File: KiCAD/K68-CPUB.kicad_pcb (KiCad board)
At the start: 2 copper layers, 100 x 100 mm, 64 parts, among them J1 PIA Con, J2 SBC68 BUS, J3 SERIAL COn, J4 Barrel_Jack_Switch, SW1 SW_SPDT, SW2 BOARD SW, SW3 ECHO SW, U1 74LS123, U10 74LS244, U11 74LS244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

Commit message: ガーバーデータ(仮) 生成
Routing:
- net GND: track 28.2 -> 613.9 mm, vias 0 -> 1
- net VCC: track 38.0 -> 432.9 mm, vias 0 -> 1
- net /D1: track 0.00 -> 259.9 mm, vias 0 -> 2
- net /D2: track 0.00 -> 223.2 mm, vias 0 -> 3
- net /D5: track 0.00 -> 212.1 mm, vias 0 -> 3
- net /~RES: track 0.00 -> 198.2 mm, vias 0 -> 3
- net /A0: track 0.00 -> 197.9 mm, vias 0 -> 2
- net /A1: track 0.00 -> 192.0 mm, vias 0 -> 1
- net /A4: track 0.00 -> 187.5 mm, vias 0 -> 4
- net /A2: track 0.00 -> 180.1 mm, vias 0 -> 2
- net /A15: track 0.00 -> 171.6 mm, vias 0 -> 2
- net /D0: track 0.00 -> 171.1 mm, vias 0 -> 4
- net /A7: track 0.00 -> 170.5 mm, vias 0 -> 4
- net /A13: track 0.00 -> 169.8 mm, vias 0 -> 4
- net /R~W: track 0.00 -> 167.3 mm, vias 0 -> 5
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- added copper zone on B.Cu, net GND
- added copper zone on F.Cu, net GND
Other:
- board text added: "28C256 (256k bit EEPROM)"
- board text added: "628128 (1M bit SRAM)"
- board text added: "74LS123"
- board text added: "74LS244"
- board text added: "74LS245"
- board text added: "MC14536"

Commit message: 基板裏面シルク追加・ガーバーデータ再作成
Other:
- board text added: "MC6800 CPU Board [K68-CPUB] REV1 KUNI-NET 2021"
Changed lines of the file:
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@@
   (general
     (thickness 1.6)
-    (drawings 18)
+    (drawings 19)
     (tracks 3065)
     (zones 0)
@@
     )
   )
+  (gr_text "MC6800 CPU Board \n[K68-CPUB] REV1\n\nKUNI-NET 2021" (at 198.5 140) (layer B.SilkS)
+    (effects (font (size 2 2) (thickness 0.2)) (justify left mirror))
+  )
   (gr_text 74LS00 (at 113.9 130.8 270) (layer F.SilkS)

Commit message: 基板パターン修正中...
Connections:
- net /DBE renamed /PH2
- net /R~W renamed /R~{W}
- net /~HALT renamed /~{HALT}
- net /~IRQ renamed /~{IRQ}
- net /~NMI renamed /~{NMI}
- net /~RAMCE renamed /~{RAMCE}
- net /~RD renamed /~{RD}
- net /~RES renamed /~{RES}
- net /~WR renamed /~{WR}
- C4 pad 1: Net-(C4-Pad1) -> Net-(U1B-RCext)
- C4 pad 2: Net-(C4-Pad2) -> Net-(U1B-Cext)
- J1 pad 1: (no net) -> unconnected-(J1-Pin_1-Pad1)
- J1 pad 2: (no net) -> unconnected-(J1-Pin_2-Pad2)
- J2 pad 10: /D7n -> /D7
- J2 pad 11: /A0n -> /A0
- J2 pad 12: /A1n -> /A1
- J2 pad 13: /A2n -> /A2
- J2 pad 14: /A3n -> /A3
- J2 pad 15: /A4n -> /A4
- J2 pad 16: /A5n -> /A5
- J2 pad 17: /A6n -> /A6
- J2 pad 18: /A7n -> /A7
- J2 pad 19: /A8n -> /A8
- J2 pad 20: /A9n -> /A9
- J2 pad 21: /A10n -> /A10
- J2 pad 22: /A11n -> /A11
- J2 pad 23: /A12n -> /A12
- J2 pad 24: /A13n -> /A13
- J2 pad 25: /A14n -> /A14
- J2 pad 26: /A15n -> /A15
- J2 pad 3: /D0n -> /D0
- J2 pad 32: (no net) -> unconnected-(J2-Pin_32-Pad32)
- J2 pad 34: (no net) -> unconnected-(J2-Pin_34-Pad34)
- J2 pad 36: (no net) -> unconnected-(J2-Pin_36-Pad36)
- J2 pad 4: /D1n -> /D1
- J2 pad 5: /D2n -> /D2
- J2 pad 6: /D3n -> /D3
- J2 pad 7: /D4n -> /D4
- J2 pad 8: /D5n -> /D5
- J2 pad 9: /D6n -> /D6
- J3 pad 2: (no net) -> unconnected-(J3-Pin_2-Pad2)
- J3 pad 3: (no net) -> unconnected-(J3-Pin_3-Pad3)
- J3 pad 4: /TxD -> /RxD
- J3 pad 5: /RxD -> /TxD
- J3 pad 6: (no net) -> unconnected-(J3-Pin_6-Pad6)
- RN1 pad 5: (no net) -> unconnected-(RN1-R4-Pad5)
- RV2 pad 2: Net-(C4-Pad2) -> Net-(U1B-RCext)
- RV2 pad 3: Net-(C4-Pad2) -> Net-(U1B-RCext)
- SW1 pad 3: (no net) -> unconnected-(SW1-C-Pad3)
- U1 pad 6: Net-(C4-Pad2) -> Net-(U1B-Cext)
- U1 pad 7: Net-(C4-Pad1) -> Net-(U1B-RCext)
- U10 pad 11: /A4 -> /A4c
- U10 pad 12: /A3n -> /A3
- U10 pad 13: /A5 -> /A5c
- U10 pad 14: /A2n -> /A2
- U10 pad 15: /A6 -> /A6c
- U10 pad 16: /A1n -> /A1
- U10 pad 17: /A7 -> /A7c
- U10 pad 18: /A0n -> /A0
- U10 pad 2: /A0 -> /A0c
- U10 pad 3: /A7n -> /A7
- U10 pad 4: /A1 -> /A1c
- U10 pad 5: /A6n -> /A6
- U10 pad 6: /A2 -> /A2c
- U10 pad 7: /A5n -> /A5
- U10 pad 8: /A3 -> /A3c
- U10 pad 9: /A4n -> /A4
- U11 pad 11: /A12 -> /A12c
- U11 pad 12: /A11n -> /A11
- U11 pad 13: /A13 -> /A13c
- U11 pad 14: /A10n -> /A10
- U11 pad 15: /A14 -> /A14c
- U11 pad 16: /A9n -> /A9
- U11 pad 17: /A15 -> /A15c
- U11 pad 18: /A8n -> /A8
- U11 pad 2: /A8 -> /A8c
- U11 pad 3: /A15n -> /A15
- U11 pad 4: /A9 -> /A9c
- U11 pad 5: /A14n -> /A14
- U11 pad 6: /A10 -> /A10c
- U11 pad 7: /A13n -> /A13
- U11 pad 8: /A11 -> /A11c
- U11 pad 9: /A12n -> /A12
- U12 pad 37: (no net) -> unconnected-(U12-~{IRQB}-Pad37)
- U12 pad 38: (no net) -> unconnected-(U12-~{IRQA}-Pad38)
- U14 pad 1: (no net) -> unconnected-(U14-NC-Pad1)
- U14 pad 31: GND -> /A15
- U15 pad 1: (no net) -> unconnected-(U15-Pad1)
- U15 pad 2: (no net) -> unconnected-(U15-Pad2)
- U15 pad 3: (no net) -> unconnected-(U15-Pad3)
- U2 pad 11: (no net) -> unconnected-(U2-Pad11)
- U4 pad 10: /A1 -> /A1c
- U4 pad 11: /A2 -> /A2c
- U4 pad 12: /A3 -> /A3c
- U4 pad 13: /A4 -> /A4c
- U4 pad 14: /A5 -> /A5c
- U4 pad 15: /A6 -> /A6c
- U4 pad 16: /A7 -> /A7c
- U4 pad 17: /A8 -> /A8c
- U4 pad 18: /A9 -> /A9c
- U4 pad 19: /A10 -> /A10c
- U4 pad 20: /A11 -> /A11c
- U4 pad 22: /A12 -> /A12c
- U4 pad 23: /A13 -> /A13c
- U4 pad 24: /A14 -> /A14c
- U4 pad 25: /A15 -> /A15c
- U4 pad 26: /D7 -> /D7c
- U4 pad 27: /D6 -> /D6c
- U4 pad 28: /D5 -> /D5c
- U4 pad 29: /D4 -> /D4c
- U4 pad 30: /D3 -> /D3c
- U4 pad 31: /D2 -> /D2c
- U4 pad 32: /D1 -> /D1c
- U4 pad 33: /D0 -> /D0c
- U4 pad 35: (no net) -> unconnected-(U4-N.C.-Pad35)
- U4 pad 38: (no net) -> unconnected-(U4-N.C.-Pad38)
- U4 pad 7: (no net) -> unconnected-(U4-BA-Pad7)
- U4 pad 9: /A0 -> /A0c
- U5 pad 11: (no net) -> unconnected-(U5-Pad11)
- U5 pad 8: (no net) -> unconnected-(U5-Pad8)
- U7 pad 12: (no net) -> unconnected-(U7-O3-Pad12)
- U7 pad 13: (no net) -> unconnected-(U7-O2-Pad13)
- U7 pad 14: (no net) -> unconnected-(U7-O1-Pad14)
- U7 pad 15: (no net) -> unconnected-(U7-O0-Pad15)
- U8 pad 11: /D7 -> /D7c
- U8 pad 12: /D6 -> /D6c
- U8 pad 13: /D5 -> /D5c
- U8 pad 14: /D4 -> /D4c
- U8 pad 15: /D3 -> /D3c
- U8 pad 16: /D2 -> /D2c
- U8 pad 17: /D1 -> /D1c
- U8 pad 18: /D0 -> /D0c
- U8 pad 2: /D0n -> /D0
- U8 pad 3: /D1n -> /D1
- U8 pad 4: /D2n -> /D2
- U8 pad 5: /D3n -> /D3
- U8 pad 6: /D4n -> /D4
- U8 pad 7: /D5n -> /D5
- U8 pad 8: /D6n -> /D6
- U8 pad 9: /D7n -> /D7
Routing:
- net GND: track 613.9 -> 0.00 mm, vias 1 -> 0
- net VCC: track 432.9 -> 0.00 mm, vias 1 -> 0
- net /D1: track 259.9 -> 0.00 mm, vias 2 -> 0
- net /D2: track 223.2 -> 0.00 mm, vias 3 -> 0
- net /D5: track 212.1 -> 0.00 mm, vias 3 -> 0
- net /~{RES}: track 198.2 -> 0.00 mm, vias 3 -> 0
- net /A0: track 197.9 -> 0.00 mm, vias 2 -> 0
- net /A1: track 192.0 -> 0.00 mm, vias 1 -> 0
- net /A4: track 187.5 -> 0.00 mm, vias 4 -> 0
- net /A2: track 180.1 -> 0.00 mm, vias 2 -> 0
- net /A15: track 171.6 -> 0.00 mm, vias 2 -> 0
- net /D0: track 171.1 -> 0.00 mm, vias 4 -> 0
- net /A7: track 170.5 -> 0.00 mm, vias 4 -> 0
- net /A13: track 169.8 -> 0.00 mm, vias 4 -> 0
- net /R~{W}: track 167.3 -> 0.00 mm, vias 5 -> 0
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- removed copper zone on B.Cu, net GND
- removed copper zone on F.Cu, net GND
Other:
- net class BOLD removed
- net class Default removed

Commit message: REV2 基板 ガーバー出力
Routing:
- net GND: track 0.00 -> 607.5 mm, vias 0 -> 6
- net VCC: track 0.00 -> 443.0 mm, vias 0 -> 1
- net /D0: track 0.00 -> 300.5 mm, vias 0 -> 4
- net /D4: track 0.00 -> 248.5 mm, vias 0 -> 4
- net /D5: track 0.00 -> 240.5 mm, vias 0 -> 3
- net /D3: track 0.00 -> 228.0 mm, vias 0 -> 4
- net /D1: track 0.00 -> 222.2 mm, vias 0 -> 2
- net /A2: track 0.00 -> 221.8 mm, vias 0 -> 1
- net /A11: track 0.00 -> 214.4 mm, vias 0 -> 3
- net /A6: track 0.00 -> 199.2 mm, vias 0 -> 7
- net /A5c: track 0.00 -> 188.8 mm, vias 0 -> 1
- net /A1: track 0.00 -> 188.1 mm, vias 0 -> 5
- net /A7c: track 0.00 -> 186.2 mm, vias 0 -> 3
- net /A10: track 0.00 -> 185.1 mm, vias 0 -> 4
- net /A0: track 0.00 -> 183.7 mm, vias 0 -> 3
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- added copper zone on B.Cu, net GND
- added copper zone on F.Cu, net GND
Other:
- board text added: "MC6800 CPU Board [K68-CPUB] REV2 KUNI-NET 2024"
- board text removed: "MC6800 CPU Board [K68-CPUB] REV1 KUNI-NET 2021"

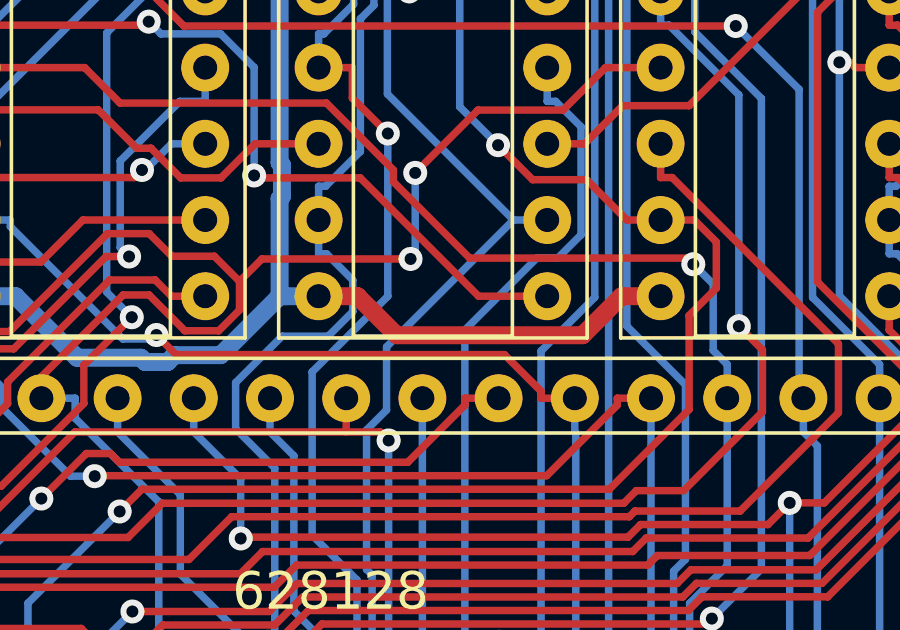
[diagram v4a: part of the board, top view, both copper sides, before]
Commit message: ビアのテンティングを変更してREV2ガーバー再出力
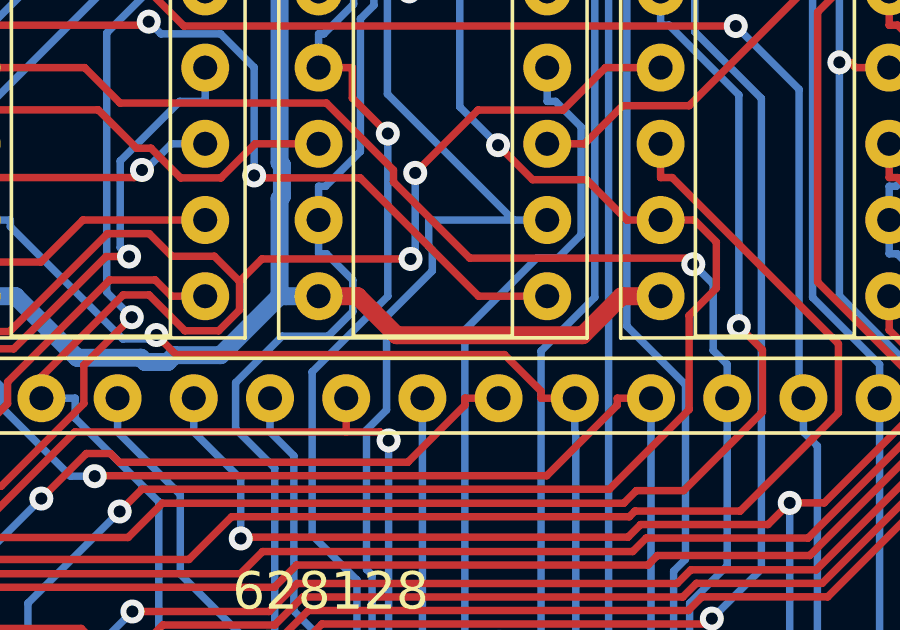
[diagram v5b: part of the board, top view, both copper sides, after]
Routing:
- net /A3: track 136.4 -> 138.2 mm
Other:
- rule pad_to_mask_clearance: 0.051 -> 0
